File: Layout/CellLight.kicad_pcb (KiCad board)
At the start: 2 copper layers, 50 x 50 mm, 40 parts, among them J1 Conn_01x03, J2 Conn_01x03, J3 Conn_01x03, J4 Conn_01x06, SW1 SW_Push, U1 DSPIC33FJ128GP802-I_SO, U2 TS3A4751PWR, U3 MB85RC256, U4 TPS562200, U5 AP2112K-3.3, U6 SN74LVC1T45DCK

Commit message: Priliminary PCB layout
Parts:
- added J5: COMM, Connector_PinSocket_2.54mm:PinSocket_1x02_P2.54mm_Vertical, F.Cu at (244.3, 121.5)
- added J6: I2C, Connector_PinSocket_2.54mm:PinSocket_1x02_P2.54mm_Vertical, F.Cu at (238.7, 121.5)
- C10, C11, C5, C7, C8, C9, D1, D2, D3, D4, R4, U5: moved to F.Cu
- J1, J2, J3: footprint Connector_PinHeader_1.00mm:PinHeader_1x03_P1.00mm_Vertical -> Connector_PinHeader_2.54mm:PinHeader_1x03_P2.54mm_Vertical
- J4: footprint Connector_PinHeader_1.00mm:PinHeader_1x06_P1.00mm_Vertical -> Connector_PinHeader_2.54mm:PinHeader_1x06_P2.54mm_Vertical
- U1: value DSPIC33FJ128GP802-I_SO -> DSPIC33FJ128MC804; footprint DSPIC33FJ128GP802:SOIC127P1030X265-28N -> Package_QFP:TQFP-44_10x10mm_P0.8mm
- U2, U3: moved to B.Cu
- moved D8 77.9 mm to (211.5, 137.4)
- moved D9 76.7 mm to (211.5, 121.9)
- moved D10 75.5 mm to (211.5, 106.4)
- moved D2 71.7 mm to (192.6, 132.9), turned to 90 degrees
- moved D1 70.3 mm to (180.1, 132.9), turned to 90 degrees
- moved D3 68.9 mm to (184.2, 132.9), turned to 270 degrees
- moved C11 66.4 mm to (200.2, 133.9), turned to 180 degrees
- moved D4 65.0 mm to (188.4, 133.0), turned to 270 degrees
- moved C5 62.3 mm to (190.4, 127.0), turned to 0 degrees
- moved C10 62.1 mm to (200.2, 132.1)
- moved C7 61.4 mm to (190.5, 125.1), turned to 0 degrees
- moved C8 60.8 mm to (182.1, 127.0), turned to 0 degrees
- moved U5 60.5 mm to (200.1, 129.2), turned to 0 degrees
- moved C9 59.8 mm to (182.1, 125.1), turned to 0 degrees
- moved L1 58.9 mm to (189.4, 128.0), turned to 270 degrees
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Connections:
- D10 pad 2: (no net) -> Net-(D10-Pad2)
- D5 pad 2: (no net) -> Net-(D5-Pad2)
- D6 pad 2: (no net) -> Net-(D6-Pad2)
- D7 pad 2: (no net) -> Net-(D7-Pad2)
- D8 pad 2: (no net) -> Net-(D8-Pad2)
- D9 pad 2: (no net) -> Net-(D9-Pad2)
- J4 pad 6: (no net) -> Net-(J4-Pad6)
- U1 pad 1: RESET -> SDA
- U1 pad 10: (no net) -> Net-(U1-Pad10)
- U1 pad 11: FRAM_WP -> Net-(U1-Pad11)
- U1 pad 12: PORT3_SEL -> Net-(U1-Pad12)
- U1 pad 13: +3V3 -> Net-(U1-Pad13)
- U1 pad 14: PORT3_IO -> Net-(U1-Pad14)
- U1 pad 15: PORT2_IO -> Net-(U1-Pad15)
- U1 pad 16: PORT1_IO -> Net-(U1-Pad16)
- U1 pad 17: SCL -> Net-(U1-Pad17)
- U1 pad 18: SDA -> RESET
- U1 pad 19: GND -> Net-(U1-Pad19)
- U1 pad 20: Net-(C1-Pad2) -> Net-(U1-Pad20)
- U1 pad 21: (no net) -> PGED
- U1 pad 22: (no net) -> PGEC
- U1 pad 23: (no net) -> Net-(U1-Pad23)
- U1 pad 24: (no net) -> Net-(U1-Pad24)
- U1 pad 25: (no net) -> IO_COM
- U1 pad 26: PWM_OUT -> IO_COM
- U1 pad 27: (no net) -> Net-(U1-Pad27)
- U1 pad 28: (no net) -> +3V3
- U1 pad 4: PGED -> PORT3_SEL
- U1 pad 5: PGEC -> Net-(U1-Pad5)
- U1 pad 6: IO_COM -> GND
- U1 pad 7: IO_COM -> Net-(C1-Pad2)
- U1 pad 8: GND -> Net-(U1-Pad8)
- U1 pad 9: (no net) -> FRAM_WP
- U2 pad 10: (no net) -> Net-(U2-Pad10)
- U2 pad 11: (no net) -> Net-(U2-Pad11)
- U2 pad 12: (no net) -> Net-(U2-Pad12)
- U5 pad 4: (no net) -> Net-(U5-Pad4)
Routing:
- net GND: track 300.1 -> 0.00 mm
- net Net-(D10-Pad4): track 167.5 -> 0.00 mm
- net +3V3: track 141.2 -> 0.00 mm, vias 1 -> 0
- net +5V: track 121.0 -> 0.00 mm, vias 1 -> 0
- net PRI_HI: track 66.3 -> 0.00 mm
- net PRI_LO: track 63.5 -> 0.00 mm
- net RESET: track 53.4 -> 0.00 mm, vias 1 -> 0
- net PGEC: track 41.5 -> 0.00 mm, vias 1 -> 0
- net PGED: track 41.0 -> 0.00 mm, vias 1 -> 0
- net PORT1_SEL: track 30.7 -> 0.00 mm
- net IO_COM: track 29.5 -> 0.00 mm
- net PORT2_SEL: track 27.8 -> 0.00 mm
- net +VDC: track 27.4 -> 0.00 mm
- net PORT3_IO: track 26.4 -> 0.00 mm, vias 1 -> 0
- net PORT1_IO: track 25.0 -> 0.00 mm, vias 1 -> 0
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- removed copper zone on B.Cu, net GND
- removed copper zone on F.Cu, net GND
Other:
- board size 50 x 50 mm -> 58.4 x 48.3 mm
- rule pad_to_mask_clearance: 0.05 -> 0

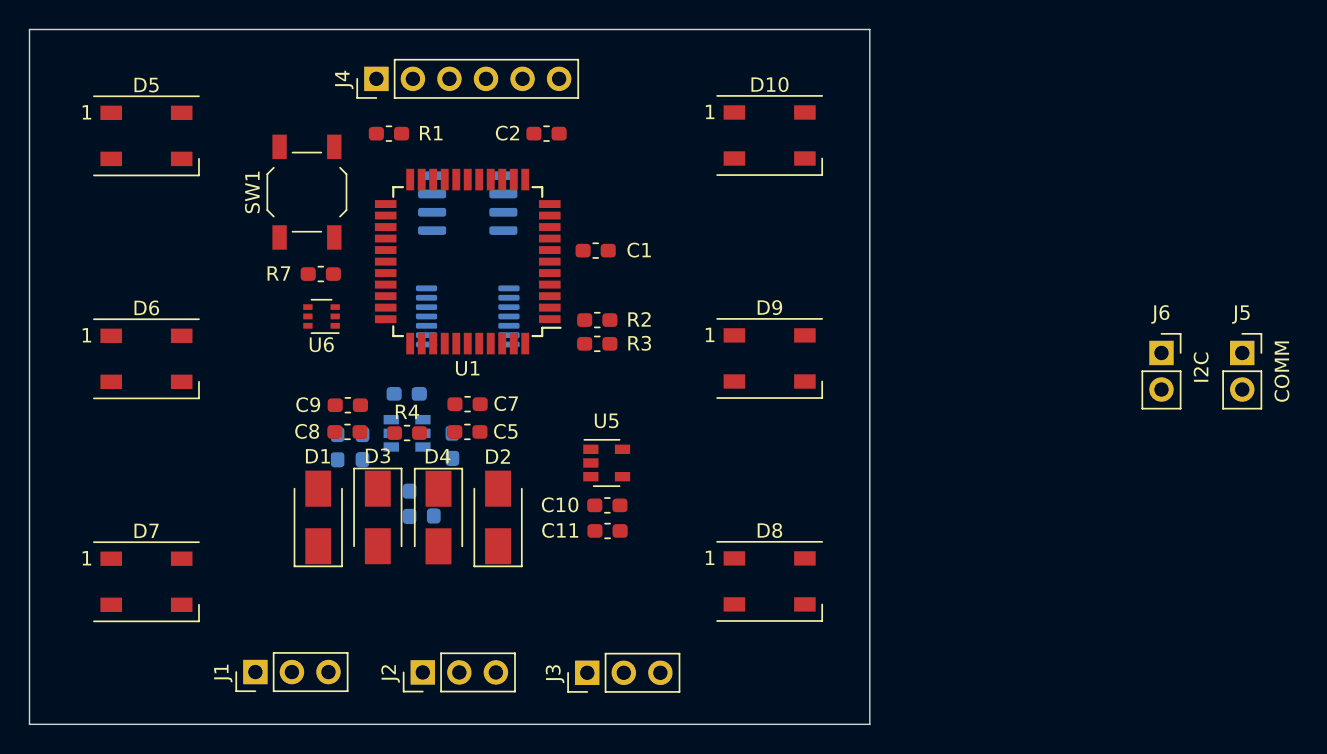
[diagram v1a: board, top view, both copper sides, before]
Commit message: Route the PCB
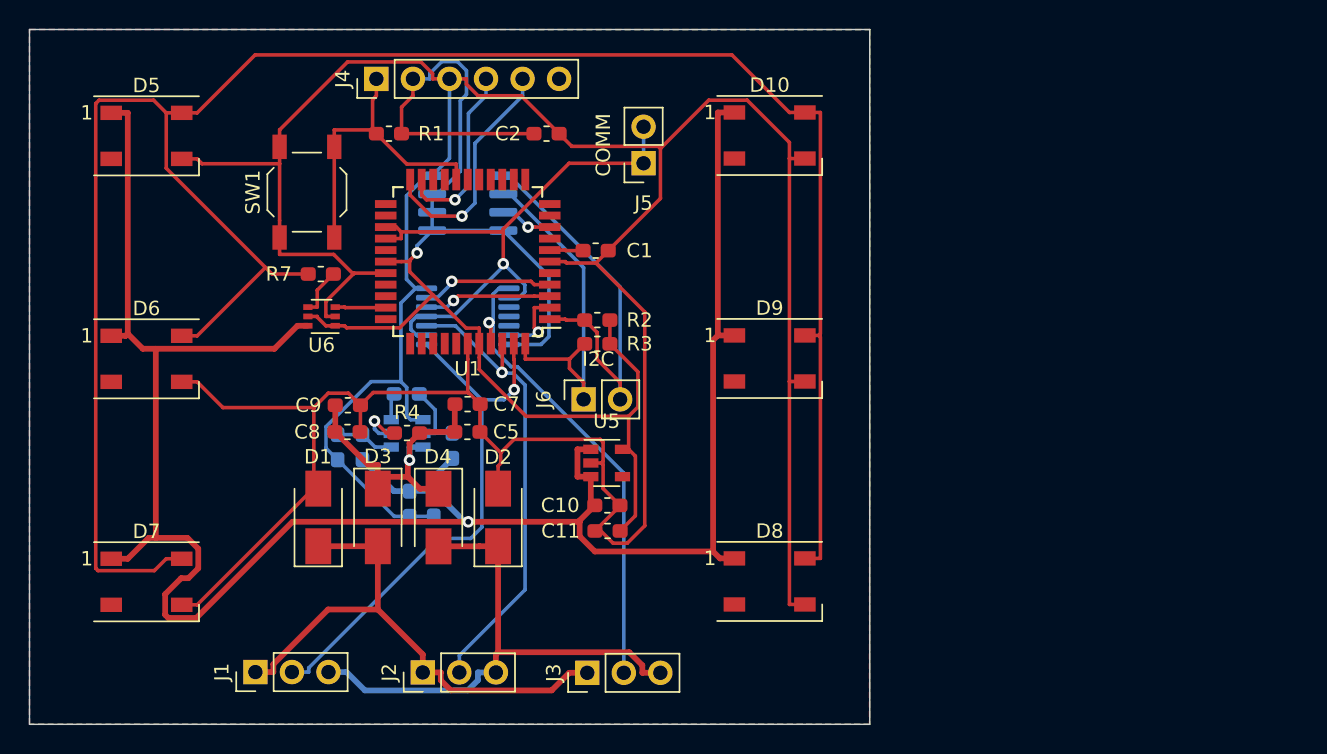
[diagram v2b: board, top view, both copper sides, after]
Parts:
- moved J5 43.6 mm to (202.7, 108.3), turned to 180 degrees
- moved J6 40.3 mm to (198.5, 124.7), turned to 90 degrees
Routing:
- net GND: track 0.00 -> 257.3 mm
- net +5V: track 0.00 -> 153.7 mm, vias 0 -> 1
- net Net-(D10-Pad4): track 0.00 -> 150.5 mm
- net +3V3: track 0.00 -> 100.0 mm, vias 0 -> 1
- net IO_COM: track 0.00 -> 40.2 mm, vias 0 -> 1
- net PRI_LO: track 0.00 -> 38.1 mm
- net PRI_HI: track 0.00 -> 37.6 mm
- net PORT1_IO: track 0.00 -> 37.6 mm, vias 0 -> 1
- net PORT3_IO: track 0.00 -> 33.4 mm, vias 0 -> 1
- net PORT2_IO: track 0.00 -> 32.4 mm, vias 0 -> 1
- net SDA: track 0.00 -> 28.1 mm
- net SCL: track 0.00 -> 25.7 mm
- net RESET: track 0.00 -> 21.7 mm
- net +VDC: track 0.00 -> 21.6 mm, vias 0 -> 1
- net PGEC: track 0.00 -> 16.6 mm, vias 0 -> 1
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- added copper zone on B.Cu, net GND
- added copper zone on F.Cu, net GND

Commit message: Layout
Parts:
- removed D10, D8, D9: WS2812B, LED_SMD:LED_WS2812B_PLCC4_5.0x5.0mm_P3.2mm
- C1, C10, C2, C5, C7, C8, C9, R1, R2, R3, R4: moved to B.Cu
- J5: value COMM -> Conn_01x01_Female; footprint Connector_PinSocket_2.54mm:PinSocket_1x02_P2.54mm_Vertical -> Connector_PinSocket_2.54mm:PinSocket_1x01_P2.54mm_Vertical
- J6: value I2C -> Conn_01x02_Female
- L1: footprint Inductor_SMD:L_0603_1608Metric_Pad1.05x0.95mm_HandSolder -> Inductor_SMD:L_Taiyo-Yuden_NR-40xx_HandSoldering
- R6, U2, U3, U4: moved to F.Cu
- moved D7 71.8 mm to (237.3, 118.2), turned to 180 degrees
- moved D6 70.1 mm to (237.3, 111.0), turned to 180 degrees
- moved D5 69.2 mm to (237.3, 103.8), turned to 180 degrees
- moved R7 47.1 mm to (227.1, 121.0), turned to 180 degrees
- moved U6 43.0 mm to (223.2, 120.4), turned to 0 degrees
- moved C4 38.2 mm to (204.4, 97.4), turned to 180 degrees
- moved C6 37.5 mm to (204.4, 99.0), turned to 180 degrees
- moved J6 36.0 mm to (224.2, 99.5), turned to 0 degrees
- moved C11 35.7 mm to (208.8, 99.2), turned to 270 degrees
- moved J4 34.6 mm to (210.6, 124.8)
- moved C10 31.7 mm to (204.4, 100.7), turned to 180 degrees
- moved R6 31.0 mm to (186.8, 97.2), turned to 180 degrees
- moved R5 30.5 mm to (187.8, 98.2), turned to 90 degrees
- moved U5 30.5 mm to (205.8, 99.2)
- moved R4 28.9 mm to (185.9, 98.2), turned to 90 degrees
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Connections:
- J1 pad 2: PORT1_IO -> PRI_LO
- J1 pad 3: PRI_LO -> PORT1_IO
- J2 pad 2: PORT2_IO -> PRI_LO
- J2 pad 3: PRI_LO -> PORT2_IO
- J3 pad 2: PORT3_IO -> PRI_LO
- J3 pad 3: PRI_LO -> PORT3_IO
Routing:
- net Net-(D10-Pad4): track 150.5 -> 25.1 mm
- net +5V: track 153.7 -> 114.4 mm
- net PORT3_SEL: track 9.21 -> 46.5 mm, vias 1 -> 0
- net PORT2_SEL: track 8.88 -> 37.5 mm, vias 1 -> 2
- net PORT1_SEL: track 5.03 -> 33.1 mm, vias 1 -> 2
- net +3V3: track 100.0 -> 119.5 mm, vias 1 -> 0
- net PRI_LO: track 38.1 -> 23.1 mm
- net PORT2_IO: track 32.4 -> 47.2 mm
- net PRI_HI: track 37.6 -> 22.9 mm
- net SDA: track 28.1 -> 15.8 mm
- net PORT3_IO: track 33.4 -> 43.3 mm, vias 1 -> 0
- net GND: track 257.3 -> 248.2 mm, vias 0 -> 1
- net PORT1_IO: track 37.6 -> 46.4 mm, vias 1 -> 2
- net PGEC: track 16.6 -> 24.2 mm
- net PGED: track 12.8 -> 20.3 mm
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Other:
- board size 58.4 x 48.3 mm -> 65 x 38 mm

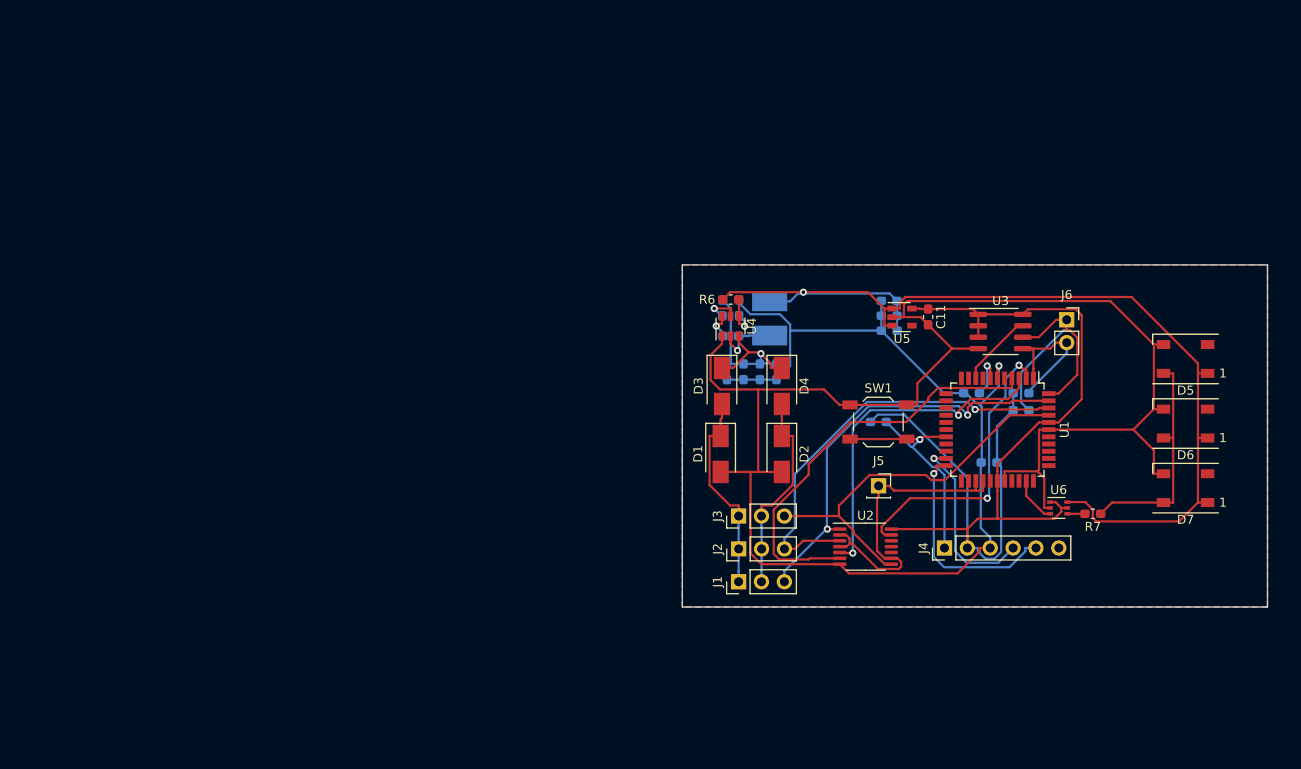
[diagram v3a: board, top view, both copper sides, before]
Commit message: Update schematic for new processor
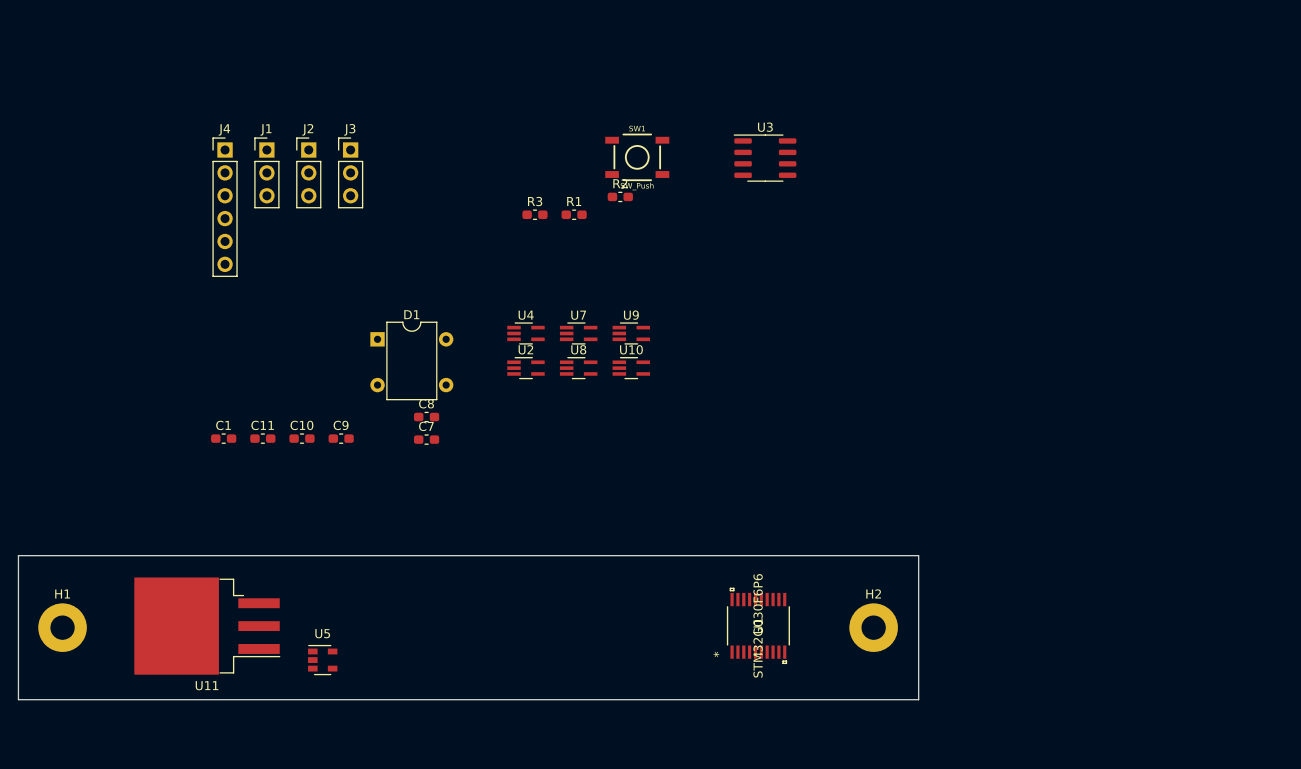
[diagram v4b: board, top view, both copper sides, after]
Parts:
- removed C2: 0.1U, Capacitor_SMD:C_0603_1608Metric_Pad1.05x0.95mm_HandSolder
- removed C3: 0.1u, Capacitor_SMD:C_0603_1608Metric_Pad1.05x0.95mm_HandSolder
- removed C4, C6: 22u, Capacitor_SMD:C_0603_1608Metric_Pad1.05x0.95mm_HandSolder
- removed C5: 10u, Capacitor_SMD:C_0603_1608Metric_Pad1.05x0.95mm_HandSolder
- removed D2, D3, D4: US1M, Diode_SMD:D_SMA
- removed D5, D6, D7: WS2812B, LED_SMD:LED_WS2812B_PLCC4_5.0x5.0mm_P3.2mm
- removed J5: Conn_01x01_Female, Connector_PinSocket_2.54mm:PinSocket_1x01_P2.54mm_Vertical
- removed J6: Conn_01x02_Female, Connector_PinSocket_2.54mm:PinSocket_1x02_P2.54mm_Vertical
- removed L1: 2.2u, Inductor_SMD:L_Taiyo-Yuden_NR-40xx_HandSoldering
- removed R4: 1k, Resistor_SMD:R_0603_1608Metric_Pad1.05x0.95mm_HandSolder
- removed R5: 9.09k, Resistor_SMD:R_0603_1608Metric_Pad1.05x0.95mm_HandSolder
- removed R6: 49.9k, Resistor_SMD:R_0603_1608Metric_Pad1.05x0.95mm_HandSolder
- removed R7: 470, Resistor_SMD:R_0603_1608Metric_Pad1.05x0.95mm_HandSolder
- removed U6: SN74LVC1T45DCK, Package_TO_SOT_SMD:SOT-363_SC-70-6
- added H1: MountingHole, MountingHole:MountingHole_2.7mm_M2.5_Pad, F.Cu at (112.6, 133.7)
- added H2: MountingHole, MountingHole:MountingHole_2.7mm_M2.5_Pad, F.Cu at (202.7, 133.7)
- added U10: 74LVC1G125, Package_TO_SOT_SMD:SOT-353_SC-70-5_Handsoldering, F.Cu at (175.8, 104.9)
- added U11: LM1085-5.0, Package_TO_SOT_SMD:TO-263-3_TabPin2, F.Cu at (128.7, 133.5)
- added U7: 74LVC1G125, Package_TO_SOT_SMD:SOT-353_SC-70-5_Handsoldering, F.Cu at (169.9, 101.0)
- added U8: 74LVC1G125, Package_TO_SOT_SMD:SOT-353_SC-70-5_Handsoldering, F.Cu at (169.9, 104.9)
- added U9: 74LVC1G125, Package_TO_SOT_SMD:SOT-353_SC-70-5_Handsoldering, F.Cu at (175.8, 101.0)
- C1: value 10U -> 4.7u; moved to F.Cu
- C10, C7, C8, C9: moved to F.Cu
- C11: value 0.1u -> 1u
- D1: value US1M -> DF02M; footprint Diode_SMD:D_SMA -> Diode_THT:Diode_Bridge_DIP-4_W7.62mm_P5.08mm
- R1: value 10k -> R_US; moved to F.Cu
- R2, R3: value 4.7k -> R_US; moved to F.Cu
- SW1: footprint Button_Switch_SMD:SW_SPST_TL3342 -> Switches:TACTILE_SWITCH_SMD_5.2MM
- U1: value DSPIC33FJ128MC804 -> STM32G030F6P6; footprint Package_QFP:TQFP-44_10x10mm_P0.8mm -> stm32g030f6p6:STM32G030F6P6
- U2: value TS3A4751PWR -> 74LVC1G125; footprint Package_SO:TSSOP-14_4.4x5mm_P0.65mm -> Package_TO_SOT_SMD:SOT-353_SC-70-5_Handsoldering
- U4: value TPS562200 -> 74LVC1G125; footprint Package_TO_SOT_SMD:SOT-23-6 -> Package_TO_SOT_SMD:SOT-353_SC-70-5_Handsoldering
- moved J4 91.3 mm to (130.7, 80.6), turned to 0 degrees
- moved C1 83.2 mm to (130.5, 112.7)
- moved C11 75.1 mm to (134.8, 112.7), turned to 0 degrees
- moved U5 74.8 mm to (141.5, 137.3)
- moved J1 71.0 mm to (135.3, 80.6), turned to 0 degrees
- moved C10 66.3 mm to (139.2, 112.7), turned to 0 degrees
- moved J2 65.1 mm to (139.9, 80.6), turned to 0 degrees
- moved J3 59.3 mm to (144.6, 80.6), turned to 0 degrees
- moved R3 58.2 mm to (165.1, 87.8)
- moved R2 49.6 mm to (174.6, 85.8)
- moved C9 48.9 mm to (143.6, 112.7), turned to 0 degrees
- moved U2 42.6 mm to (164.1, 104.9)
- moved R1 40.9 mm to (169.4, 87.8)
- moved D1 40.2 mm to (147.6, 101.7), turned to 0 degrees
- moved SW1 39.8 mm to (176.4, 81.5)
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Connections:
- net Net-(U1-Pad15) renamed LED_OUT
- net Net-(U1-Pad19) renamed /Processor/SWCLK
- C1 pad 1: GND -> +3V3
- C1 pad 2: Net-(C1-Pad2) -> GND
- D1 pad 1: PRI_HI -> +VDC
- R1 pad 1: +3V3 -> 3.3V
- R1 pad 2: RESET -> /Processor/RESET
- R2 pad 1: +3V3 -> 3.3V
- R2 pad 2: SDA -> SCL
- R3 pad 1: +3V3 -> 3.3V
- R3 pad 2: SCL -> SDA
- SW1 pad 2: RESET -> /Processor/RESET
- U1 pad 1: SDA -> SCL
- U1 pad 11: Net-(U1-Pad11) -> CH3_RX_EN
- U1 pad 12: Net-(U1-Pad12) -> CH3_TX_EN
- U1 pad 13: Net-(U1-Pad13) -> CH2_RX_EN
- U1 pad 14: Net-(U1-Pad14) -> CH2_TX_EN
- U1 pad 16: Net-(U1-Pad16) -> CH1_RX_EN
- U1 pad 17: Net-(U1-Pad17) -> CH1_TX_EN
- U1 pad 18: RESET -> /Processor/SWDIO
- U1 pad 2: PORT1_SEL -> SDA
- U1 pad 20: Net-(U1-Pad20) -> COM_DATA
- U1 pad 3: PORT2_SEL -> Net-(U1-Pad3)
- U1 pad 4: PORT3_SEL -> 3.3V
- U1 pad 5: Net-(U1-Pad5) -> GND
- U1 pad 6: GND -> /Processor/RESET
- U1 pad 7: Net-(C1-Pad2) -> CH1_DATA
- U1 pad 8: Net-(U1-Pad8) -> CH2_DATA
- U1 pad 9: FRAM_WP -> CH3_DATA
- U2 pad 1: PORT1_IO -> CH1_TX_EN
- U2 pad 2: IO_COM -> COM_DATA
- U2 pad 3: PORT2_IO -> GND
- U2 pad 4: IO_COM -> CH1_DATA
- U2 pad 5: PORT2_SEL -> 3.3V
- U4 pad 1: GND -> CH1_RX_EN
- U4 pad 2: Net-(C3-Pad1) -> CH1_DATA
- U4 pad 3: +VDC -> GND
- U4 pad 4: Net-(R5-Pad1) -> COM_DATA
- U4 pad 5: Net-(R4-Pad1) -> 3.3V
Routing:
- net GND: track 248.2 -> 0.00 mm, vias 1 -> 0
- net +3V3: track 119.5 -> 0.00 mm
- net +5V: track 114.4 -> 0.00 mm, vias 1 -> 0
- net PORT2_IO: track 47.2 -> 0.00 mm, vias 1 -> 0
- net PORT3_SEL: track 46.5 -> 0.00 mm
- net PORT1_IO: track 46.4 -> 0.00 mm, vias 2 -> 0
- net PORT3_IO: track 43.3 -> 0.00 mm
- net PORT2_SEL: track 37.5 -> 0.00 mm, vias 2 -> 0
- net IO_COM: track 35.0 -> 0.00 mm
- net PORT1_SEL: track 33.1 -> 0.00 mm, vias 2 -> 0
- net SCL: track 29.3 -> 0.00 mm
- net RESET: track 29.0 -> 0.00 mm, vias 1 -> 0
- net Net-(D10-Pad4): track 25.1 -> 0.00 mm
- net +VDC: track 24.8 -> 0.00 mm, vias 1 -> 0
- net PGEC: track 24.2 -> 0.00 mm, vias 1 -> 0
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- removed copper zone on B.Cu, net GND
- removed copper zone on F.Cu, net GND
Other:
- board size 65 x 38 mm -> 100 x 16 mm
